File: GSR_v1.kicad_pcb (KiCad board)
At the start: 2 copper layers, 32.2 x 20.5 mm, 62 parts, among them P1 CONN_2, P2 CONN_2, P3 CONN_2, P4 CONN_2, Q1 DMP21D5UFB4-7B, U1 TPS63001, U2 LM324N, U3 NRF528XX-QFAA, U4 TMP116, U5 TPS2294x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

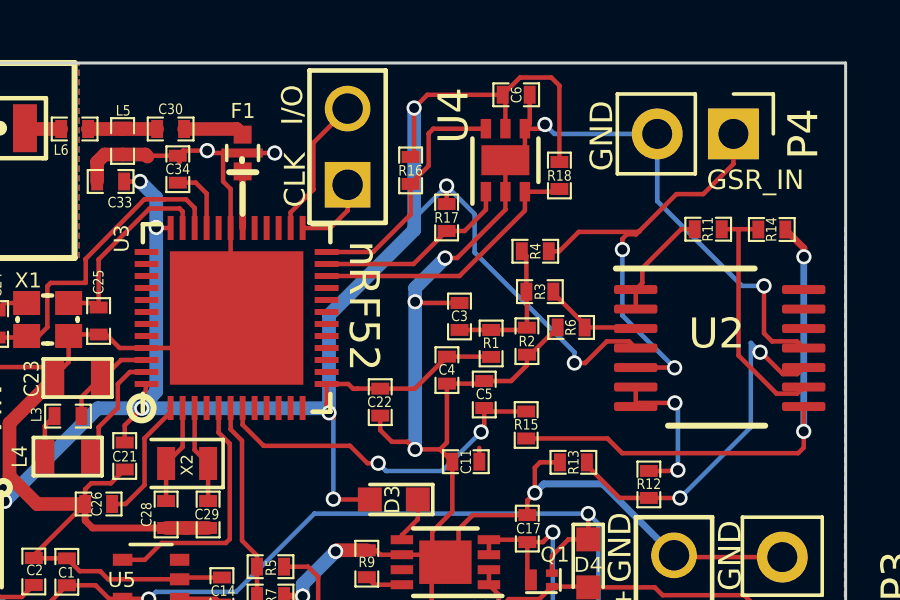
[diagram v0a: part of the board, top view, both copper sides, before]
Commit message: moved connectors for Temp sensor down to make space for uSD card
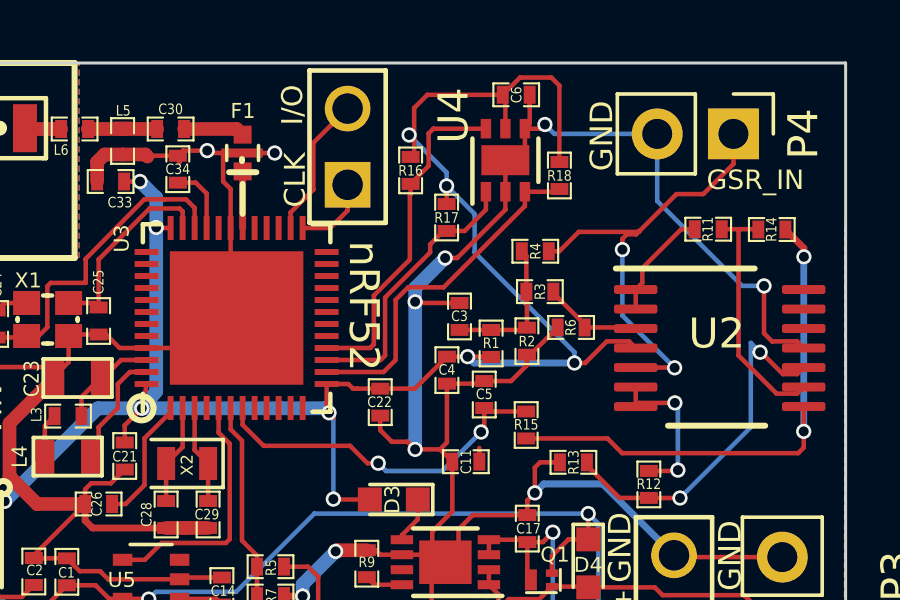
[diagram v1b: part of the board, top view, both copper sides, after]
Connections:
- U3 pad 14: Net-(U3-Pad14) -> /ALERT
- U3 pad 15: Net-(U3-Pad15) -> /SCL
- U3 pad 16: Net-(U3-Pad16) -> /SDA
- U3 pad 22: /ALERT -> Net-(U3-Pad22)
- U3 pad 23: /SCL -> Net-(U3-Pad23)
- U3 pad 24: /SDA -> Net-(U3-Pad24)
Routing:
- net DVDD: track 76.1 -> 69.0 mm, vias 9 -> 10
- net /SDA: track 8.49 -> 11.4 mm
- net /SCL: track 6.66 -> 9.27 mm
- net /ALERT: track 9.33 -> 11.7 mm

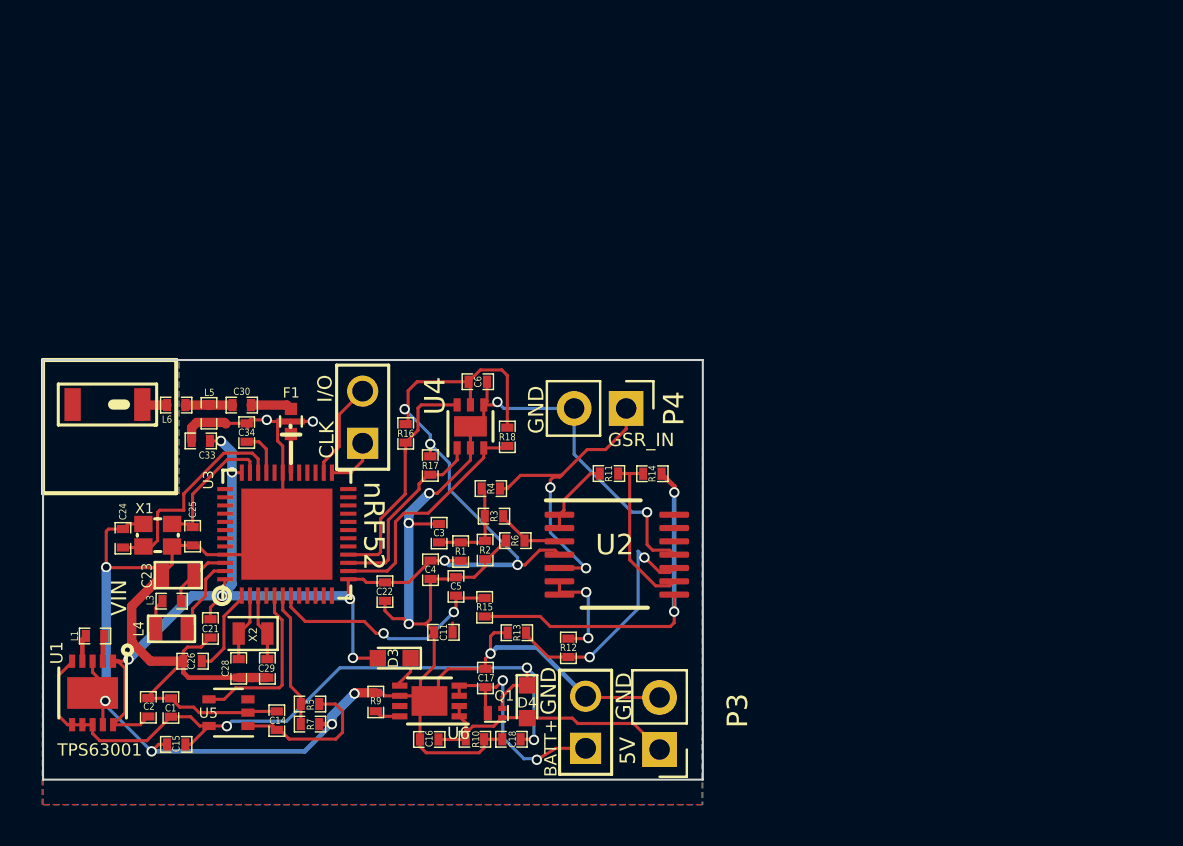
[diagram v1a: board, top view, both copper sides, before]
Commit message: Added microSD Card to sch and pcb
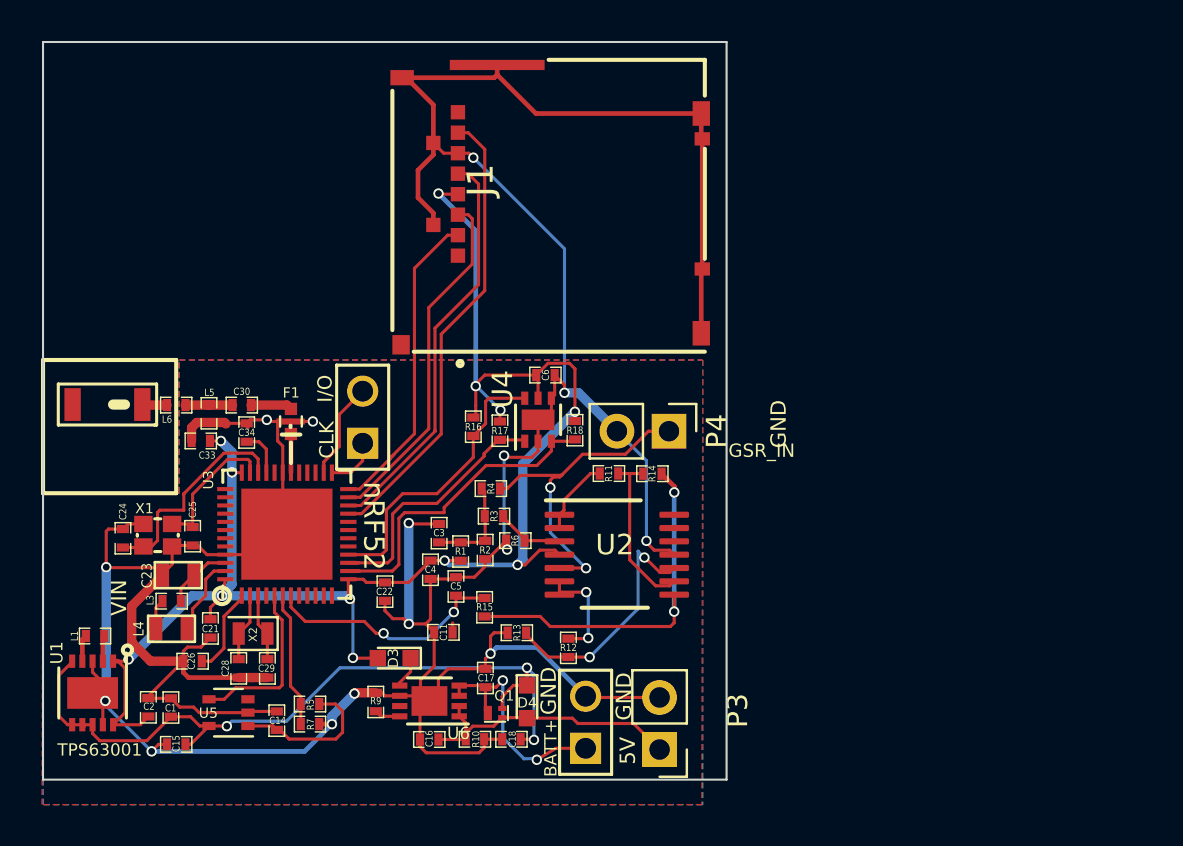
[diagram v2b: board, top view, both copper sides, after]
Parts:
- added J1: Micro_SD_Card_Det, musaPwrPad:SCHA4B0419, F.Cu at (282.9, 110.8)
- moved R17 3.80 mm to (288.2, 128.9)
- moved U4 3.32 mm to (290.1, 128.4)
- moved C6 3.32 mm to (290.4, 126.2)
- moved R18 3.32 mm to (291.9, 128.9)
- moved R16 3.32 mm to (286.9, 128.8)
- moved P4 2.37 mm to (296.4, 129.0)
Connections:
- R18 pad 1: /ALERT -> Net-(R18-Pad1)
- U3 pad 21: Net-(U3-Pad21) -> /DAT0_MISO
- U3 pad 22: Net-(U3-Pad22) -> /uSD_CLK
- U3 pad 23: Net-(U3-Pad23) -> /CMD_MOSI
- U3 pad 24: Net-(U3-Pad24) -> /DAT3_CS
- U4 pad 3: /ALERT -> Net-(R18-Pad1)
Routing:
- net DGND: track 163.7 -> 214.1 mm, vias 13 -> 15
- net /DAT0_MISO: track 0.00 -> 22.6 mm
- net /uSD_CLK: track 0.00 -> 20.0 mm
- net /CMD_MOSI: track 0.00 -> 17.2 mm
- net /DAT3_CS: track 0.00 -> 15.8 mm
- net DVDD: track 69.0 -> 80.3 mm, vias 10 -> 12
- net /ALERT: track 11.7 -> 15.6 mm
- net /SCL: track 9.27 -> 13.0 mm
- net /SDA: track 11.4 -> 14.2 mm
- net /ELECTRODE_INPUT: track 15.4 -> 16.5 mm
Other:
- board size 32.2 x 20.5 mm -> 33.4 x 36 mm

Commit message: Added ground plane under micoSD slot
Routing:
- added copper zone on B.Cu, net (none)
- added copper zone on F.Cu, net (none)
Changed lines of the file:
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@@
     (connect_pads (clearance 0.508))
     (min_thickness 0.254)
-    (fill (arc_segments 16) (thermal_gap 0.508) (thermal_bridge_width 0.508))
+    (fill yes (arc_segments 16) (thermal_gap 0.508) (thermal_bridge_width 0.508))
     (polygon
       (pts
@@
     (connect_pads (clearance 0.508))
     (min_thickness 0.254)
-    (fill (arc_segments 16) (thermal_gap 0.508) (thermal_bridge_width 0.508))
+    (fill yes (arc_segments 16) (thermal_gap 0.508) (thermal_bridge_width 0.508))
     (polygon
       (pts
@@
       )
     )
+  )
+  (zone (net 0) (net_name "") (layer F.Cu) (hatch edge 0.508)
+    (connect_pads (clearance 0.508))
+    (min_thickness 0.254)
+    (fill yes (arc_segments 16) (thermal_gap 0.508) (thermal_bridge_width 0.508))
+    (polygon
+      (pts
+        (xy 282.3 110.21) (xy 299.01 110.21) (xy 299.01 125.34) (xy 282.3 125.33)
+      )
+    )
+  )
+  (zone (net 0) (net_name "") (layer B.Cu) (hatch edge 0.508)
+    (connect_pads (clearance 0.508))
+    (min_thickness 0.254)
+    (fill yes (arc_segments 16) (thermal_gap 0.508) (thermal_bridge_width 0.508))
+    (polygon
+      (pts
+        (xy 282.3 110.21) (xy 299.01 110.21) (xy 299.01 125.34) (xy 282.3 125.33)
+      )
+    )

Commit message: Slight tweaking, set fills to DGND.
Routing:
- removed copper zone on B.Cu, net (none)
- removed copper zone on F.Cu, net (none)
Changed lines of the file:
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@@
   )
   (setup
-    (last_trace_width 0.229)
+    (last_trace_width 0.4572)
     (user_trace_width 0.152)
     (user_trace_width 0.229)
@@
     (effects (font (size 0.762 0.762) (thickness 0.127)) (justify mirror))
   )
-  (segment (start 287.9215 111.7225) (end 288.065 111.579) (width 0.229) (layer F.Cu) (net 36))
-  (segment (start 283.425 111.7225) (end 287.9215 111.7225) (width 0.229) (layer F.Cu) (net 36))
-  (segment (start 288.065 111.579) (end 288.065 111.1) (width 0.229) (layer F.Cu) (net 36))
-  (segment (start 289.956 113.47) (end 288.065 111.579) (width 0.229) (layer F.Cu) (net 36))
-  (segment (start 298.025 113.47) (end 289.956 113.47) (width 0.229) (layer F.Cu) (net 36))
-  (segment (start 298.075 121.0575) (end 298.075 114.7075) (width 0.229) (layer F.Cu) (net 36))
-  (segment (start 298.025 114.6575) (end 298.075 114.7075) (width 0.229) (layer F.Cu) (net 36))
-  (segment (start 298.025 113.47) (end 298.025 114.6575) (width 0.229) (layer F.Cu) (net 36))
-  (segment (start 298.025 121.1075) (end 298.075 121.0575) (width 0.229) (layer F.Cu) (net 36))
-  (segment (start 298.025 124.195) (end 298.025 121.1075) (width 0.229) (layer F.Cu) (net 36))
   (segment (start 274.1 140.2) (end 273.64958 140.2) (width 0.152) (layer F.Cu) (net 1))
   (segment (start 274.73 139.57) (end 274.1 140.2) (width 0.152) (layer F.Cu) (net 1))
@@
   (segment (start 285.125 132.5) (end 283.475 132.5) (width 0.152) (layer F.Cu) (net 35))
   (segment (start 283.475 132.5) (end 282.963189 133.011811) (width 0.152) (layer F.Cu) (net 35))
+  (segment (start 287.9215 111.7225) (end 288.065 111.579) (width 0.229) (layer F.Cu) (net 36))
+  (segment (start 283.425 111.7225) (end 287.9215 111.7225) (width 0.229) (layer F.Cu) (net 36))
+  (segment (start 288.065 111.579) (end 288.065 111.1) (width 0.229) (layer F.Cu) (net 36))
+  (segment (start 289.956 113.47) (end 288.065 111.579) (width 0.229) (layer F.Cu) (net 36))
+  (segment (start 298.025 113.47) (end 289.956 113.47) (width 0.229) (layer F.Cu) (net 36))
+  (segment (start 298.075 121.0575) (end 298.075 114.7075) (width 0.229) (layer F.Cu) (net 36))
+  (segment (start 298.025 114.6575) (end 298.075 114.7075) (width 0.229) (layer F.Cu) (net 36))
+  (segment (start 298.025 113.47) (end 298.025 114.6575) (width 0.229) (layer F.Cu) (net 36))
+  (segment (start 298.025 121.1075) (end 298.075 121.0575) (width 0.229) (layer F.Cu) (net 36))
+  (segment (start 298.025 124.195) (end 298.025 121.1075) (width 0.229) (layer F.Cu) (net 36))
   (via (at 283.75 138.38) (size 0.508) (drill 0.3302) (layers F.Cu B.Cu) (net 36))
   (segment (start 290.06 129.465) (end 290.06 128.815) (width 0.152) (layer F.Cu) (net 36))
@@
   (segment (start 296.71 131.67042) (end 296.08958 131.05) (width 0.229) (layer F.Cu) (net 58))
   (segment (start 296.71 131.96) (end 296.71 131.67042) (width 0.229) (layer F.Cu) (net 58))
-  (segment (start 280.9 131.8) (end 280.95 131.8) (width 0.152) (layer F.Cu) (net 70))
-  (segment (start 280.9 131.8) (end 281.1 131.8) (width 0.1524) (layer F.Cu) (net 70))
   (segment (start 289.41 127.365) (end 287.66 127.365) (width 0.152) (layer F.Cu) (net 61))
   (segment (start 287.5 128.60458) (end 286.9 129.20458) (width 0.152) (layer F.Cu) (net 61))
@@
   (segment (start 286.85 118.6055) (end 286.652 118.4075) (width 0.152) (layer F.Cu) (net 69))
   (segment (start 286.85 120.818622) (end 286.85 118.6055) (width 0.152) (layer F.Cu) (net 69))
+  (segment (start 280.9 131.8) (end 280.95 131.8) (width 0.152) (layer F.Cu) (net 70))
+  (segment (start 280.9 131.8) (end 281.1 131.8) (width 0.1524) (layer F.Cu) (net 70))
   (segment (start 280.8 131.8) (end 281.352 131.8) (width 0.152) (layer F.Cu) (net 70))
   (segment (start 284.028401 121.027099) (end 284.028401 129.096599) (width 0.152) (layer F.Cu) (net 70))
@@
     (polygon
       (pts
-        (xy 298.05 147.2) (xy 265.85 147.2) (xy 265.9 132) (xy 272.55 132) (xy 272.55 125.5)
-        (xy 298.1 125.5)
+        (xy 299.04 125.5) (xy 298.1 125.5) (xy 298.05 147.2) (xy 265.85 147.2) (xy 265.9 132)
+        (xy 272.55 132) (xy 272.55 125.5) (xy 282.33 125.5) (xy 282.3 110.21) (xy 299.01 110.21)
       )
     )
@@
     )
   )
-  (zone (net 0) (net_name "") (layer F.Cu) (hatch edge 0.508)
+  (zone (net 36) (net_name DGND) (layer B.Cu) (hatch edge 0.508)
     (connect_pads (clearance 0.508))
     (min_thickness 0.254)
@@
     (polygon
       (pts
-        (xy 282.3 110.21) (xy 299.01 110.21) (xy 299.01 125.34) (xy 282.3 125.33)
+        (xy 282.3 110.2) (xy 299.01 110.2) (xy 299.04 125.49) (xy 282.33 125.49)
       )
     )
-  )
-  (zone (net 0) (net_name "") (layer B.Cu) (hatch edge 0.508)
-    (connect_pads (clearance 0.508))
-    (min_thickness 0.254)
-    (fill yes (arc_segments 16) (thermal_gap 0.508) (thermal_bridge_width 0.508))
-    (polygon
-      (pts
-        (xy 282.3 110.21) (xy 299.01 110.21) (xy 299.01 125.34) (xy 282.3 125.33)
-      )
-    )

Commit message: Updated Gerber files, fixed back silkscreen
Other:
- board text added: "nRF52-GSR Prototype 01/09/2019 Yeo GaTech BNE Lab"
- board text removed: "nRF52-GSR Prototype 09/03/18 Yeo GaTech BNE Lab"
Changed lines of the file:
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@@
   )
   (gr_line (start 269.9 127.673) (end 269.32 127.673) (angle 90) (layer F.SilkS) (width 0.5))
-  (gr_text "nRF52-GSR Prototype \n09/03/18\nYeo GaTech BNE Lab" (at 273.36 141.38) (layer B.SilkS)
+  (gr_text "nRF52-GSR Prototype \n01/09/2019\nYeo GaTech BNE Lab" (at 273.36 141.38) (layer B.SilkS)
     (effects (font (size 0.762 0.762) (thickness 0.127)) (justify mirror))
   )

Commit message: Replaced through-hole footprints with pads.
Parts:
- P1, P2: footprint PIN_ARRAY_2X1 -> musaPwrPad:SMDPad_1x02_P2.54mm
- P3, P4: footprint Pin_Headers:Pin_Header_Straight_1x02_Pitch2.54mm -> musaPwrPad:SMDPad_1x02_P2.54mm
- moved P1 1.30 mm to (292.4, 144.5), turned to 180 degrees
- moved P2 1.12 mm to (281.6, 129.4), turned to 180 degrees
- moved P4 0.11 mm to (296.4, 128.9)
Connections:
- R18 pad 1: Net-(R18-Pad1) -> /ALERT
- U4 pad 3: Net-(R18-Pad1) -> /ALERT
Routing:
- net DGND: track 214.1 -> 187.4 mm, vias 15 -> 17

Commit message: Updated schematic, and footprints. PCB needs arrangement and routing.
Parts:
- added C10: 10uF, SM0402, F.Cu at (305.8, 145.0)
- added C7: 0.1uF, SM0402, F.Cu at (317.5, 137.7)
- added C8: 0.1uF, SM0402, F.Cu at (319.1, 137.9)
- added C9: 10uF, SM0402, F.Cu at (304.2, 144.8)
- added IC1: AD5242BRUZ1M, SOP65P640X120-16N, F.Cu at (309.8, 133.4)
- added L2: 4.7uH, SM0603, F.Cu at (314.9, 144.0)
- added U7: ADS1220, Package_DFN_QFN:QFN-16-1EP_3x3mm_P0.5mm_EP1.8x1.8mm, F.Cu at (317.7, 133.8)
- added U8: TPS61222, Package_TO_SOT_SMD:SOT-363_SC-70-6, F.Cu at (309.1, 144.3)
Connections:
- net /SCL renamed /TMP_SCL
- net /SDA renamed /TMP_SDA
- C3 pad 2: Net-(C3-Pad2) -> /RT_1
- C5 pad 2: /GSR_AIN -> /ADC_AIN0
- R1 pad 1: Net-(C3-Pad2) -> /RT_1
- R15 pad 1: /GSR_AIN -> /ADC_AIN0
- R2 pad 2: Net-(C3-Pad2) -> /RT_1
- R3 pad 2: Net-(C3-Pad2) -> /RT_1
- U3 pad 7: /GSR_AIN -> Net-(U3-Pad7)
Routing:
- net /GSR_AIN: track 12.0 -> 0.00 mm, vias 2 -> 0
- net /ADC_AIN0: track 0.00 -> 1.45 mm
